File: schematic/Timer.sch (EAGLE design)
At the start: 30 parts, among them IC1 MEGA8-AI, J1 AVR_SPI_PRG_6NS, Q1 BC807-40SMD, Q2 BC807-40SMD, Q3 BC807-40SMD, Q4 BC807-40SMD

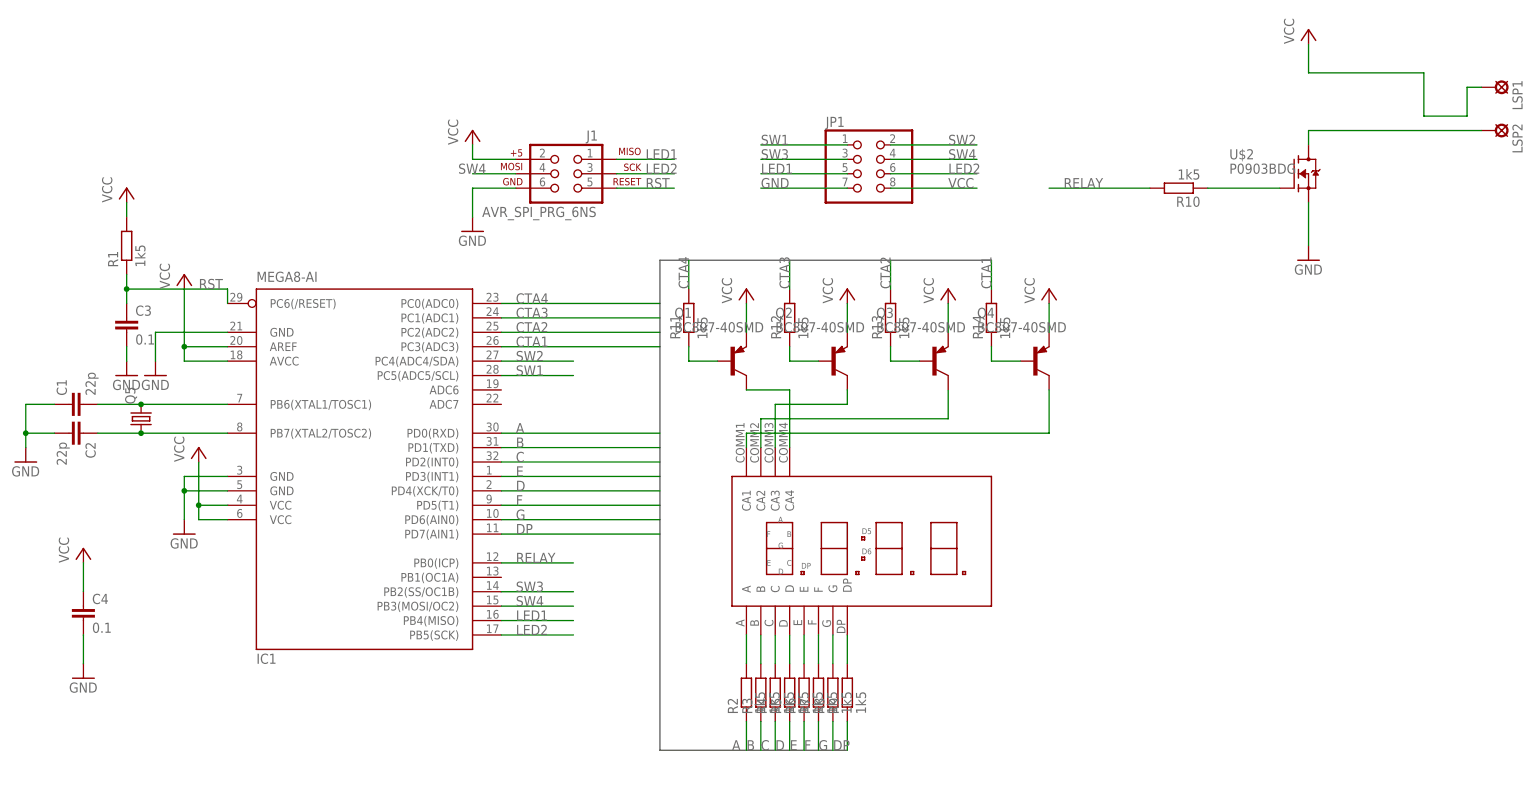
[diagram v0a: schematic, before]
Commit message: изменения в схеме
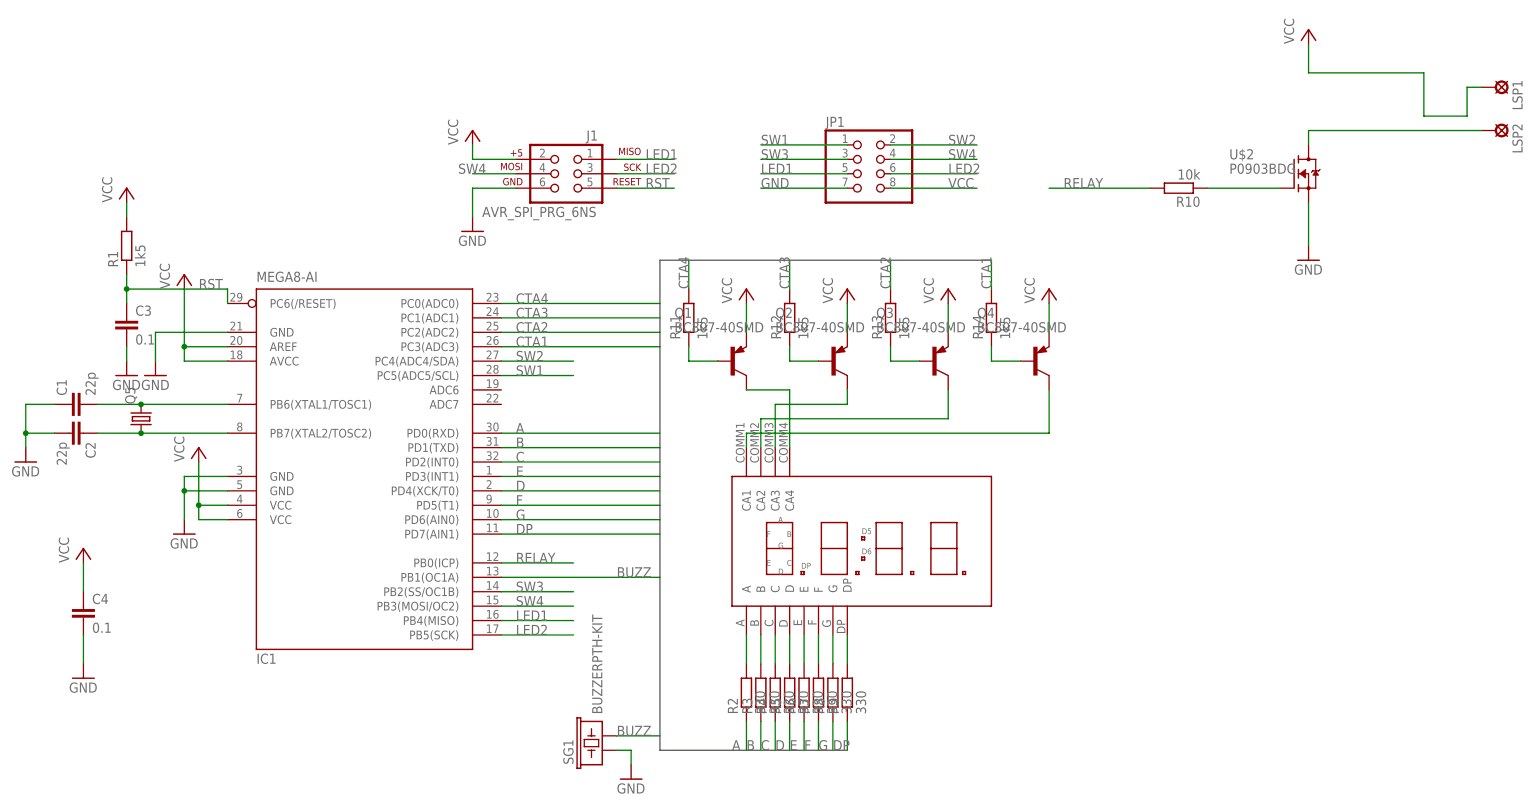
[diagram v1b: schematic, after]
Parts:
- added SG1: BUZZERPTH-KIT, SparkFun-Electromechanical:BUZZERPTH-KIT
- R10: value 1k5 -> 10k
- R2, R3, R4, R5, R6, R7, R8, R9: value 1k5 -> 330
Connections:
- new net BUZZ: IC1.PB1(OC1A), SG1.2
- net GND: now also SG1.1
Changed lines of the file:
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@@
 <setting verticaltext="up"/>
 </settings>
-<grid distance="0.1" unitdist="inch" unit="inch" style="lines" multiple="1" display="yes" altdistance="0.01" altunitdist="inch" altunit="inch"/>
+<grid distance="0.1" unitdist="inch" unit="inch" style="lines" multiple="1" display="no" altdistance="0.01" altunitdist="inch" altunit="inch"/>
 <layers>
 <layer number="1" name="Top" color="4" fill="1" visible="no" active="no"/>
@@
 <part name="R1" library="rcl" deviceset="R-EU_" device="R1206" value="1k5"/>
 <part name="GND4" library="supply1" deviceset="GND" device=""/>
-<part name="R2" library="rcl" deviceset="R-EU_" device="R1206" value="1k5"/>
-<part name="R3" library="rcl" deviceset="R-EU_" device="R1206" value="1k5"/>
-<part name="R4" library="rcl" deviceset="R-EU_" device="R1206" value="1k5"/>
-<part name="R5" library="rcl" deviceset="R-EU_" device="R1206" value="1k5"/>
-<part name="R6" library="rcl" deviceset="R-EU_" device="R1206" value="1k5"/>
-<part name="R7" library="rcl" deviceset="R-EU_" device="R1206" value="1k5"/>
-<part name="R8" library="rcl" deviceset="R-EU_" device="R1206" value="1k5"/>
-<part name="R9" library="rcl" deviceset="R-EU_" device="R1206" value="1k5"/>
+<part name="R2" library="rcl" deviceset="R-EU_" device="R1206" value="330"/>
+<part name="R3" library="rcl" deviceset="R-EU_" device="R1206" value="330"/>
+<part name="R4" library="rcl" deviceset="R-EU_" device="R1206" value="330"/>
+<part name="R5" library="rcl" deviceset="R-EU_" device="R1206" value="330"/>
+<part name="R6" library="rcl" deviceset="R-EU_" device="R1206" value="330"/>
+<part name="R7" library="rcl" deviceset="R-EU_" device="R1206" value="330"/>
+<part name="R8" library="rcl" deviceset="R-EU_" device="R1206" value="330"/>
+<part name="R9" library="rcl" deviceset="R-EU_" device="R1206" value="330"/>
 <part name="J1" library="SparkFun-Connectors" deviceset="AVR_SPI_PRG_6" device="NS"/>
 <part name="GND5" library="supply1" deviceset="GND" device=""/>
@@
 <part name="GND6" library="supply1" deviceset="GND" device=""/>
 <part name="P+9" library="supply1" deviceset="VCC" device=""/>
-<part name="R10" library="rcl" deviceset="R-EU_" device="R1206" value="1k5"/>
+<part name="R10" library="rcl" deviceset="R-EU_" device="R1206" value="10k"/>
 <part name="LSP1" library="solpad" deviceset="SE13" device=""/>
 <part name="LSP2" library="solpad" deviceset="SE13" device=""/>
@@
 <part name="P+10" library="supply1" deviceset="VCC" device=""/>
 <part name="GND7" library="supply1" deviceset="GND" device=""/>
+<part name="SG1" library="SparkFun-Electromechanical" deviceset="BUZZER" device="PTH-KIT"/>
+<part name="GND8" library="supply1" deviceset="GND" device=""/>
 </parts>
 <sheets>
@@
 <instance part="P+10" gate="VCC" x="-99.06" y="-40.64"/>
 <instance part="GND7" gate="1" x="-99.06" y="-63.5"/>
+<instance part="SG1" gate="G$1" x="-7.62" y="-76.2" rot="R90"/>
+<instance part="GND8" gate="1" x="-2.54" y="-81.28"/>
 </instances>
 <busses>
@@
 <pinref part="C4" gate="G$1" pin="2"/>
 <wire x1="-99.06" y1="-60.96" x2="-99.06" y2="-55.88" width="0.1524" layer="91"/>
+</segment>
+<segment>
+<pinref part="SG1" gate="G$1" pin="1"/>
+<pinref part="GND8" gate="1" pin="GND"/>
+<wire x1="-5.08" y1="-76.2" x2="-2.54" y2="-76.2" width="0.1524" layer="91"/>
+<wire x1="-2.54" y1="-76.2" x2="-2.54" y2="-78.74" width="0.1524" layer="91"/>
 </segment>
 </net>
@@
 </segment>
 </net>
+<net name="BUZZ" class="0">
+<segment>
+<pinref part="SG1" gate="G$1" pin="2"/>
+<wire x1="-5.08" y1="-73.66" x2="2.54" y2="-73.66" width="0.1524" layer="91"/>
+<label x="-5.08" y="-73.66" size="1.778" layer="95"/>
+</segment>
+<segment>
+<pinref part="IC1" gate="G$1" pin="PB1(OC1A)"/>
+<wire x1="-25.4" y1="-45.72" x2="2.54" y2="-45.72" width="0.1524" layer="91"/>
+<label x="-5.08" y="-45.72" size="1.778" layer="95"/>
+</segment>
+</net>
